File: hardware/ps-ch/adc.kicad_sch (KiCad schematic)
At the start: 4 parts, among them U14 ADS1118IDGS

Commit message: did some wiring
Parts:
- added C71, C72, C73, C74: C, symbol Device:C
- added R37, R69, R70, R71: R, symbol Device:R
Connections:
- net AIN0: now also R37.1; no longer U14.4 (AIN0)
- net AIN1: now also R69.1; no longer U14.5 (AIN1)
- net AIN2: now also R70.1; no longer U14.6 (AIN2)
- net AIN3: now also R71.1; no longer U14.7 (AIN3)
- net GND: now also C71.2, C72.2, C73.2, C74.2
- new net: C72.1, R70.2, U14.6 (AIN2)
- new net: C73.1, R69.2, U14.5 (AIN1)
- new net: C74.1, R37.2, U14.4 (AIN0)
- new net: C71.1, R71.2, U14.7 (AIN3)
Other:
- note added: "ADC"
- moved on the sheet: C58, C59, R41, U14

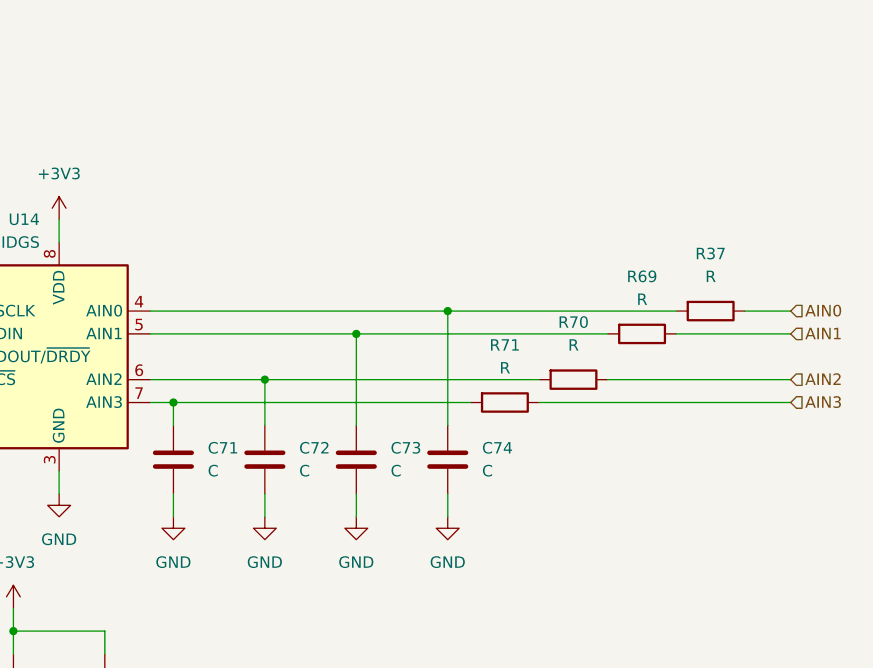
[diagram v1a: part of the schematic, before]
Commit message: added 74LVC126A
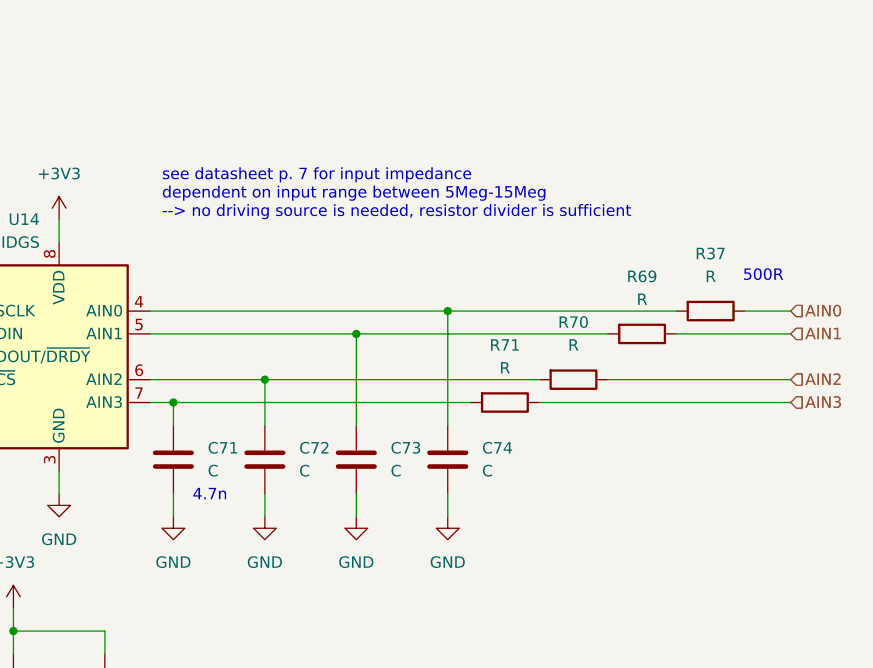
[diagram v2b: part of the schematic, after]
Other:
- note added: "4.7n"
- note added: "500R"
- note added: "see datasheet p. 7 for input impedance dependent on input range between 5Meg-15Meg --> no driving source is needed, resistor divider is sufficient"
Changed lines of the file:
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@@
 	(generator_version "9.0")
 	(paper "A4")
+	(text "500R"
+		(exclude_from_sim no)
+		(at 210.312 82.55 0)
+		(effects
+			(font
+				(size 1.27 1.27)
+			)
+		)
+	)
+	(text "see datasheet p. 7 for input impedance\ndependent on input range between 5Meg-15Meg\n--> no driving source is needed, resistor divider is sufficient"
+		(exclude_from_sim no)
+		(at 143.51 73.406 0)
+		(effects
+			(font
+				(size 1.27 1.27)
+			)
+			(justify left)
+		)
+	)
 	(text "ADC"
 		(exclude_from_sim no)
@@
 			)
 		)
+	)
+	(text "4.7n"
+		(exclude_from_sim no)
+		(at 148.844 106.934 0)
+		(effects
+			(font
+				(size 1.27 1.27)
+			)
+		)

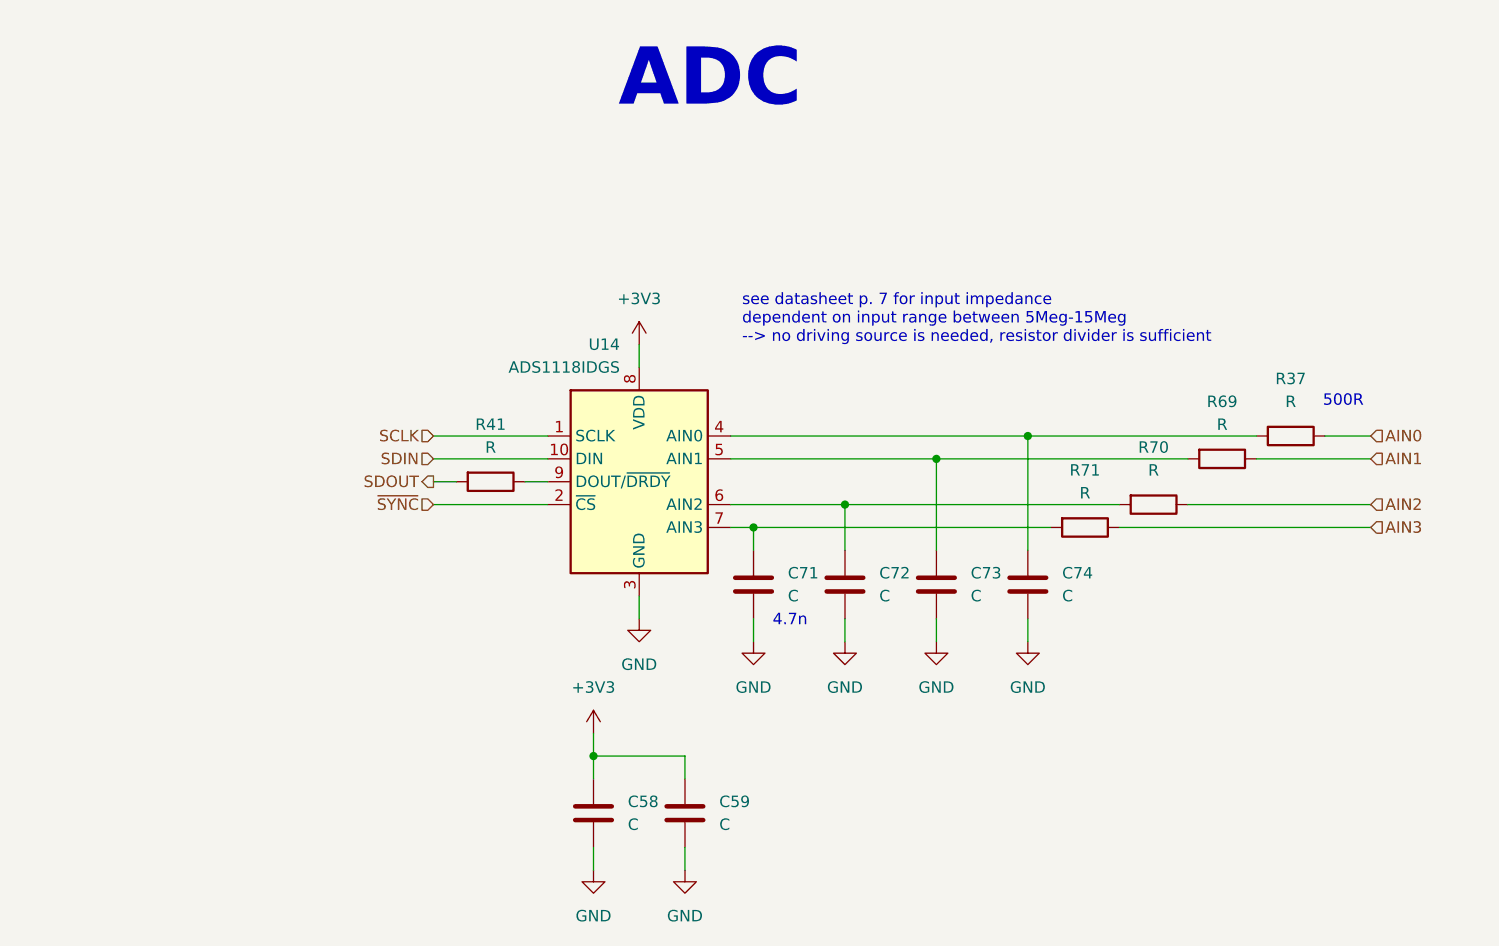
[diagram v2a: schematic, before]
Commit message: wired adc/added resolutions
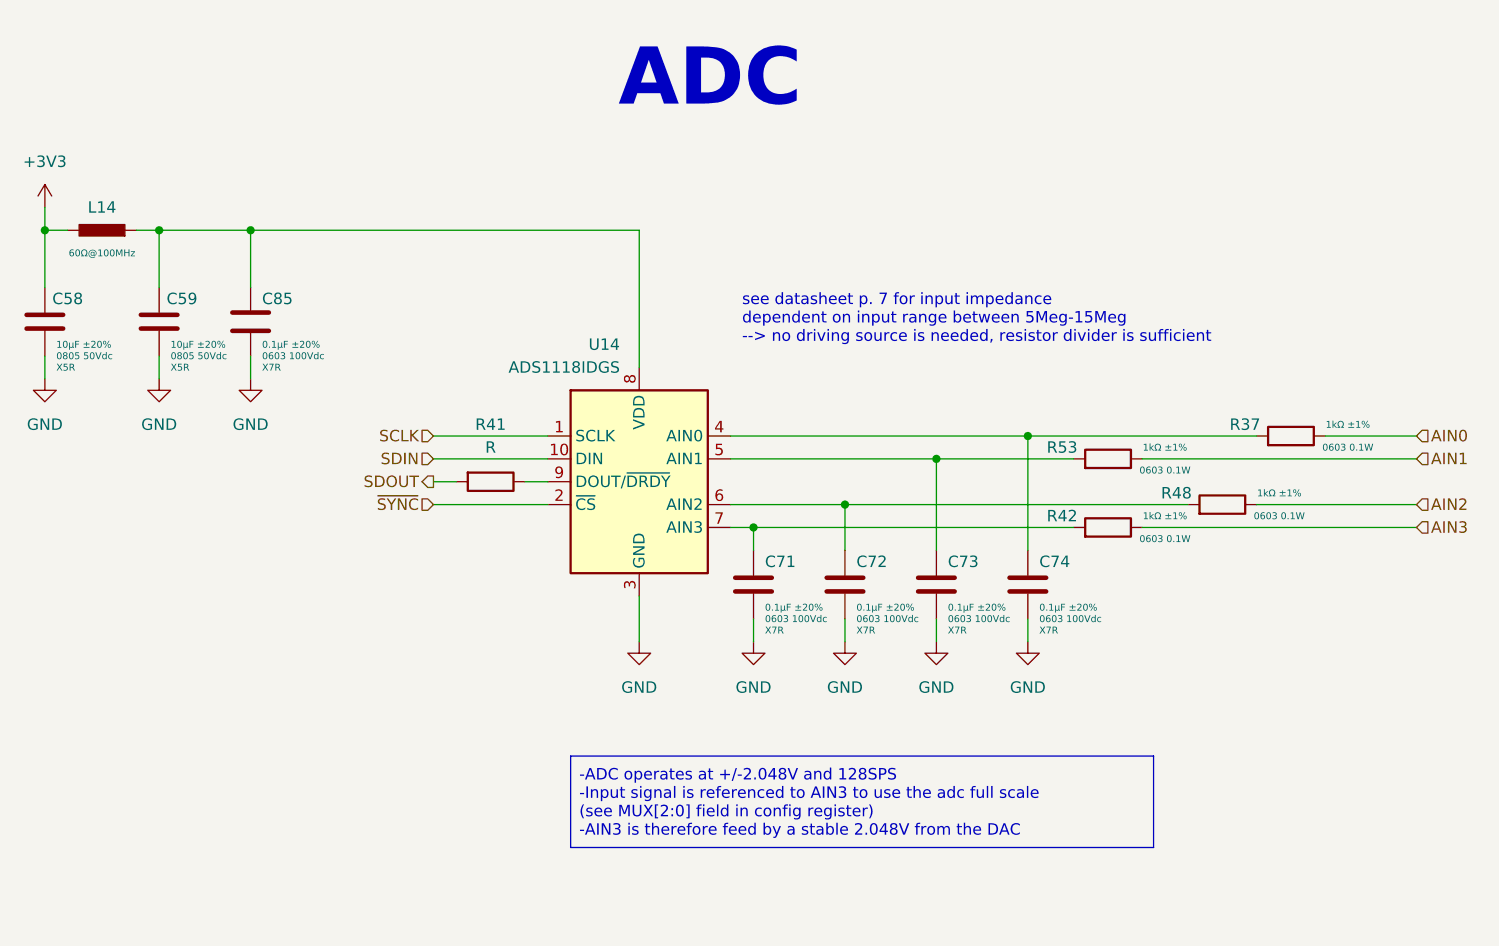
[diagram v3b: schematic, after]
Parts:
- removed C58, C59, C71, C72, C73, C74: C, symbol Device:C
- removed R37, R69, R70, R71: R, symbol Device:R
- added C58, C59: 10μF 0805 50Vdc X5R ±20%, Capacitor_SMD:C_0805_2012Metric, symbol ps-ch:10μF 0805 50Vdc X5R ±20%
- added C71, C72, C73, C74, C85: 0.1μF 0603 100Vdc X7R ±20%, Capacitor_SMD:C_0603_1608Metric, symbol ps-ch:0.1μF 0603 100Vdc X7R ±20%
- added L14: 60Ω@100MHz, Inductor_SMD:L_0603_1608Metric, symbol ps-ch:74437349015
- added R37, R42, R48, R53: 1kΩ 0603 0.1W ±1% ±100ppm/°C, Resistor_SMD:R_0603_1608Metric, symbol ps-ch:1kΩ 0603 0.1W ±1% ±100ppm/°C
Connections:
- net +3V3: now also C58.2, L14.2; no longer U14.8 (VDD)
- net AIN0: now also R37.1
- net AIN1: now also R53.1
- net AIN2: now also R48.1
- net AIN3: now also R42.1
- net GND: now also C58.1, C59.1, C71.1, C72.1, C73.1, C74.1, C85.1
- net at U14.6 (AIN2): now also C72.2, R48.2
- net at U14.5 (AIN1): now also C73.2, R53.2
- net at U14.4 (AIN0): now also C74.2, R37.2
- net at U14.7 (AIN3): now also C71.2, R42.2
- new net: C59.2, C85.2, L14.1, U14.8 (VDD)
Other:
- note removed: "4.7n"
- note removed: "500R"

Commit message: improved circuit
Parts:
- R41: value R -> 22Ω 0402 0.063W ±1% ±100ppm/°C; footprint (none) -> Resistor_SMD:R_0402_1005Metric; symbol Device:R -> ps-ch:22Ω 0402 0.063W ±1% ±100ppm/°C; DisplayValue0 (none) -> 22Ω ±1%; DisplayValue1 (none) -> 0402 0.063W; DisplayValue2 (none) -> ±100ppm; Manufacturer (none) -> Yageo; Manufacturer Part Number (none) -> AC0402FR-0722RL
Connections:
- net SDOUT: now also R41.1; no longer R41.2
- net at U14.9 (DOUT/~{DRDY}): now also R41.2; no longer R41.1
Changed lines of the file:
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@@
 	)
 	(symbol
-		(lib_id "Device:R")
+		(lib_id "ps-ch:22Ω 0402 0.063W ±1% ±100ppm/°C")
 		(at 115.57 91.44 270)
 		(unit 1)
@@
 		(on_board yes)
 		(dnp no)
-		(fields_autoplaced yes)
 		(property "Reference" "R41"
-			(at 115.57 85.09 90)
+			(at 115.57 95.25 90)
 			(effects
 				(font
@@
 			)
 		)
-		(property "Value" "R"
-			(at 115.57 87.63 90)
+		(property "Value" "22Ω 0402 0.063W ±1% ±100ppm/°C"
+			(at 130.81 91.44 0)
 			(effects
 				(font
 					(size 1.27 1.27)
 				)
+				(hide yes)
 			)
 		)
-		(property "Footprint" ""
-			(at 115.57 89.662 90)
+		(property "Footprint" "Resistor_SMD:R_0402_1005Metric"
+			(at 125.73 91.44 0)
 			(effects
 				(font
@@
 		)
 		(property "Datasheet" "~"
-			(at 115.57 91.44 0)
+			(at 115.57 91.44 90)
+			(effects
+				(font
+					(size 1 1)
+				)
+				(hide yes)
+			)
+		)
+		(property "Description" "R 0402 0.063W ±1% ±100ppm/°C"
+			(at 128.27 91.44 0)
 			(effects
 				(font
@@
 			)
 		)
-		(property "Description" "Resistor"
-			(at 115.57 91.44 0)
+		(property "Manufacturer" "Yageo"
+			(at 135.89 91.44 0)
 			(effects
 				(font
@@
 			)
 		)
+		(property "Manufacturer Part Number" "AC0402FR-0722RL"
+			(at 133.35 91.44 0)
+			(effects
+				(font
+					(size 1.27 1.27)
+				)
+				(hide yes)
+			)
+		)
+		(property "DisplayValue0" "22Ω ±1%"
+			(at 115.57 97.79 90)
+			(effects
+				(font
+					(size 0.762 0.762)
+				)
+			)
+		)
+		(property "DisplayValue1" "0402 0.063W"
+			(at 115.57 99.06 90)
+			(effects
+				(font
+					(size 0.762 0.762)
+				)
+			)
+		)
+		(property "DisplayValue2" "±100ppm"
+			(at 115.57 100.33 90)
+			(effects
+				(font
+					(size 0.762 0.762)
+				)
+			)
+		)

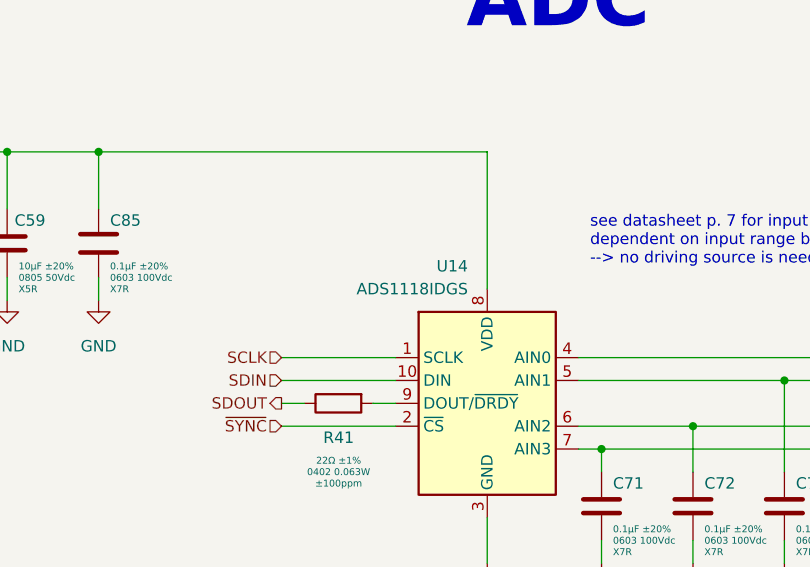
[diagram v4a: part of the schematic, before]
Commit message: assigned footprints
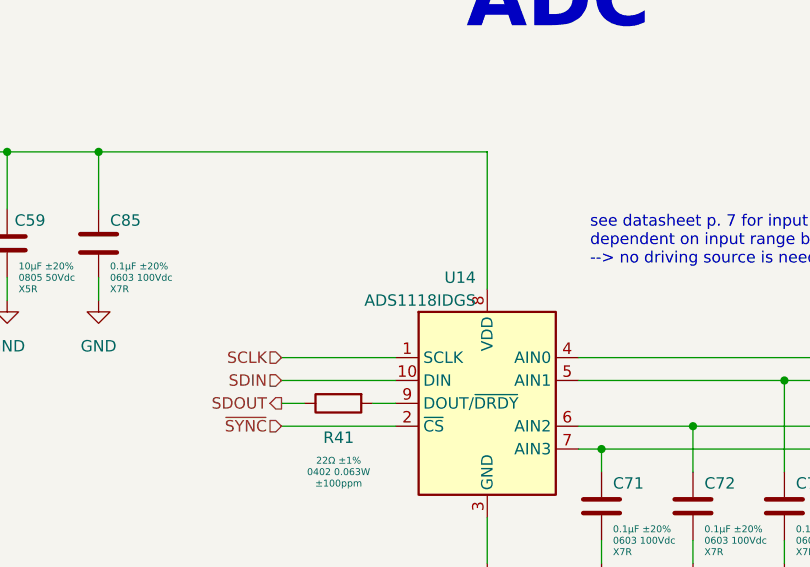
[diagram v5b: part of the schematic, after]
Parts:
- U14: footprint (none) -> Package_SO:VSSOP-10_3x3mm_P0.5mm; symbol Analog_ADC:ADS1118IDGS -> ps-ch:ADS1118IDGS; Manufacturer (none) -> Texas Instruments; Manufacturer Part Number (none) -> ADS1118IDGSR
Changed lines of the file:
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@@
 	)
 	(symbol
-		(lib_id "Analog_ADC:ADS1118IDGS")
+		(lib_id "ps-ch:ADS1118IDGS")
 		(at 132.08 91.44 0)
 		(mirror y)
@@
 		(dnp no)
 		(property "Reference" "U14"
-			(at 129.9367 76.2 0)
+			(at 130.81 77.47 0)
 			(effects
 				(font
@@
 		)
 		(property "Value" "ADS1118IDGS"
-			(at 129.9367 78.74 0)
+			(at 130.81 80.01 0)
 			(effects
 				(font
@@
 			)
 		)
-		(property "Footprint" ""
-			(at 133.35 92.71 0)
+		(property "Footprint" "Package_SO:VSSOP-10_3x3mm_P0.5mm"
+			(at 132.08 66.04 0)
 			(effects
 				(font
@@
 		)
 		(property "Datasheet" "http://www.ti.com/lit/ds/symlink/ads1118.pdf"
-			(at 154.94 81.28 0)
+			(at 132.08 60.96 0)
 			(effects
 				(font
@@
 		)
 		(property "Description" "Ultrasmall, Low-Power, SPI-Compatible, 16-Bit Analog-to-Digital Converter with Internal Reference and Temperature Sensor, VSSOP-10"
-			(at 132.08 91.44 0)
+			(at 132.08 63.5 0)
 			(effects
 				(font
+					(size 1.27 1.27)
+				)
+				(hide yes)
+			)
+		)
+		(property "Manufacturer" "Texas Instruments"
+			(at 132.08 55.88 0)
+			(effects
+				(font
+					(size 1.27 1.27)
+				)
+				(hide yes)
+			)
+		)
+		(property "Manufacturer Part Number" "ADS1118IDGSR"
+			(at 132.08 58.42 0)
+			(effects
+				(font
